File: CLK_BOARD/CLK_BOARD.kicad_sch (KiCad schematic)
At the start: 0 parts

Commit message: updated the symbol in LO board from lmx2582 to lmx2592 in order to cover the upper range of the 5Ghz spectrum. drop in replacement
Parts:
- added C1, C4: 10uF, Capacitor_SMD:C_0603_1608Metric, symbol Device:C
- added C10, C11, C15, C16, C17, C33, C9: 0.1uF, symbol Device:C
- added C12, C31, C7: 10uF, symbol Device:C
- added C13, C32, C8: 1uF, symbol Device:C
- added C14, C18, C19, C22, C23, C24, C25: 10nF, symbol Device:C
- added C2, C30, C5: 0.1uF, Capacitor_SMD:C_0603_1608Metric, symbol Device:C
- added C20, C21, C26, C27: 15pF, symbol Device:C
- added C28, C6: 1uF, Capacitor_SMD:C_0603_1608Metric, symbol Device:C
- added C29: 10nF, Capacitor_SMD:C_0603_1608Metric, symbol Device:C
- added C3: 10nF, Capacitor_SMD:C_0402_1005Metric, symbol Device:C
- added J1: PWR, Connector_PinHeader_2.54mm:PinHeader_1x02_P2.54mm_Vertical, symbol Connector_Generic:Conn_01x02
- added J2, J3, J4, J5, J8: OUT_100M_1, symbol Connector:Conn_Coaxial
- added J6: OUT_100M_3, symbol Connector:Conn_Coaxial
- added J7: OUT_100M_2, symbol Connector:Conn_Coaxial
- added J9: CTRL, symbol Connector_Generic:Conn_01x02
- added R1: 3k16, Resistor_SMD:R_0402_1005Metric, symbol Device:R
- added R10, R11, R12, R5, R6, R7, R9: 43, symbol Device:R
- added R13: 1, Resistor_SMD:R_0603_1608Metric, symbol Device:R
- added R14, R15, R16, R3, R4, R8: 0, symbol Device:R
- added R2: 1k, Resistor_SMD:R_0402_1005Metric, symbol Device:R
- added R26, R27: 10k, Resistor_SMD:R_0603_1608Metric, symbol Device:R
- added U1: TPS7A9101DSKR, Snapeda:DSK0010A, symbol Snapeda:TPS7A9101DSKR
- added U2, U3: LMK00804BPW, Snapeda:PW16_TEX-L, symbol Snapeda:LMK00804BPW
- added U4: SN74LVC1G74DCUR, Snapeda:DCU0008A_L, symbol Snapeda:SN74LVC1G74DCUR
- added X1: TB612-100.0M, Snapeda:TB612_CNW, symbol Snapeda:TB612-100.0M
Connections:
- new net: C28.1, C29.1, C30.1, R13.2, X1.9 (VCC)
- new net: R15.1, U4.7 (PRE_N)
- new net: C13.1, C15.1, C16.1, C17.1, R4.2, U3.11 (VDDO), U3.15 (VDDO), U3.3 (VDD)
- new net: C18.1, J3.1 (In)
- new net: C21.1, R8.2, U4.1 (CLK)
- new net: C19.1, J4.1 (In)
- new net: R7.1, U2.12 (Q2)
- new net: C19.2, R7.2
- new net: C26.1, R14.1, X1.5 (OUTPUT)
- new net: C23.2, J6.1 (In)
- new net: C3.2, R1.2, R2.1, U1.3 (FB)
- new net: C10.1, C11.1, C8.1, C9.1, R3.2, U2.11 (VDDO), U2.15 (VDDO), U2.3 (VDD)
- new net: R5.1, U2.16 (Q0)
- new net: C14.2, R5.2
- new net: C18.2, R6.2
- new net: C25.1, R12.2
- new net: C25.2, J8.1 (In)
- new net: C20.1, R8.1, U3.16 (Q0)
- new net: C32.1, C33.1, R16.2, U4.8 (VCC)
- new net: R9.1, U2.10 (Q3)
- new net: C22.2, R9.2
- new net: C23.1, R10.2
- new net: C24.2, J7.1 (In)
- new net: R11.1, U3.12 (Q2)
- new net: C24.1, R11.2
- new net: C1.1, C2.1, J1.2 (Pin_2), U1.10 (IN), U1.6 (SS_CTRL), U1.7 (EN), U1.9 (IN)
- new net: R12.1, U3.14 (Q1)
- new net: C22.1, J5.1 (In)
- new net: U2.8 (LVCMOS_CLK), U4.2 (D), U4.3 (Q_N)
- new net: C6.1, U1.8 (NR_SS)
- new net: R10.1, U3.10 (Q3)
- new net: R6.1, U2.14 (Q1)
- new net: C14.1, J2.1 (In)
- new net +3V3: C12.1, C3.1, C31.1, C4.1, C5.1, C7.1, R1.1, R13.1, R15.2, R16.1, R26.2, R27.2, R3.1, R4.1, U1.1 (OUT), U1.2 (OUT)
- new net GND: C1.2, C10.2, C11.2, C12.2, C13.2, C15.2, C16.2, C17.2, C2.2, C20.2, C21.2, C26.2, C27.2, C28.2, C29.2, C30.2, C31.2, C32.2, C33.2, C4.2, C5.2, C6.2, C7.2, C8.2, C9.2, J1.1 (Pin_1), J2.2 (Ext), J3.2 (Ext), J4.2 (Ext), J5.2 (Ext), J6.2 (Ext), J7.2 (Ext), J8.2 (Ext), R2.2, U1.11 (PAD), U1.4 (GND), U1.5 (PG), U2.1 (GND), U2.13 (GND), U2.7 (CLK_SEL), U2.9 (GND), U3.1 (GND), U3.13 (GND), U3.7 (CLK_SEL), U3.9 (GND), U4.4 (GND), X1.4 (GND)
- new net OSC_OUT: C27.1, R14.2, U3.8 (LVCMOS_CLK)
- new net nMUTE: J9.1 (Pin_1), R26.1, U2.4 (CLK_EN), U3.4 (CLK_EN)
- new net nRST: J9.2 (Pin_2), R27.1, U4.6 (CLR_N)
- no-connect marks 0 -> 8
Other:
- note added: "POWER SUPPLY SECTION"
- note added: "TCXO SECTION"

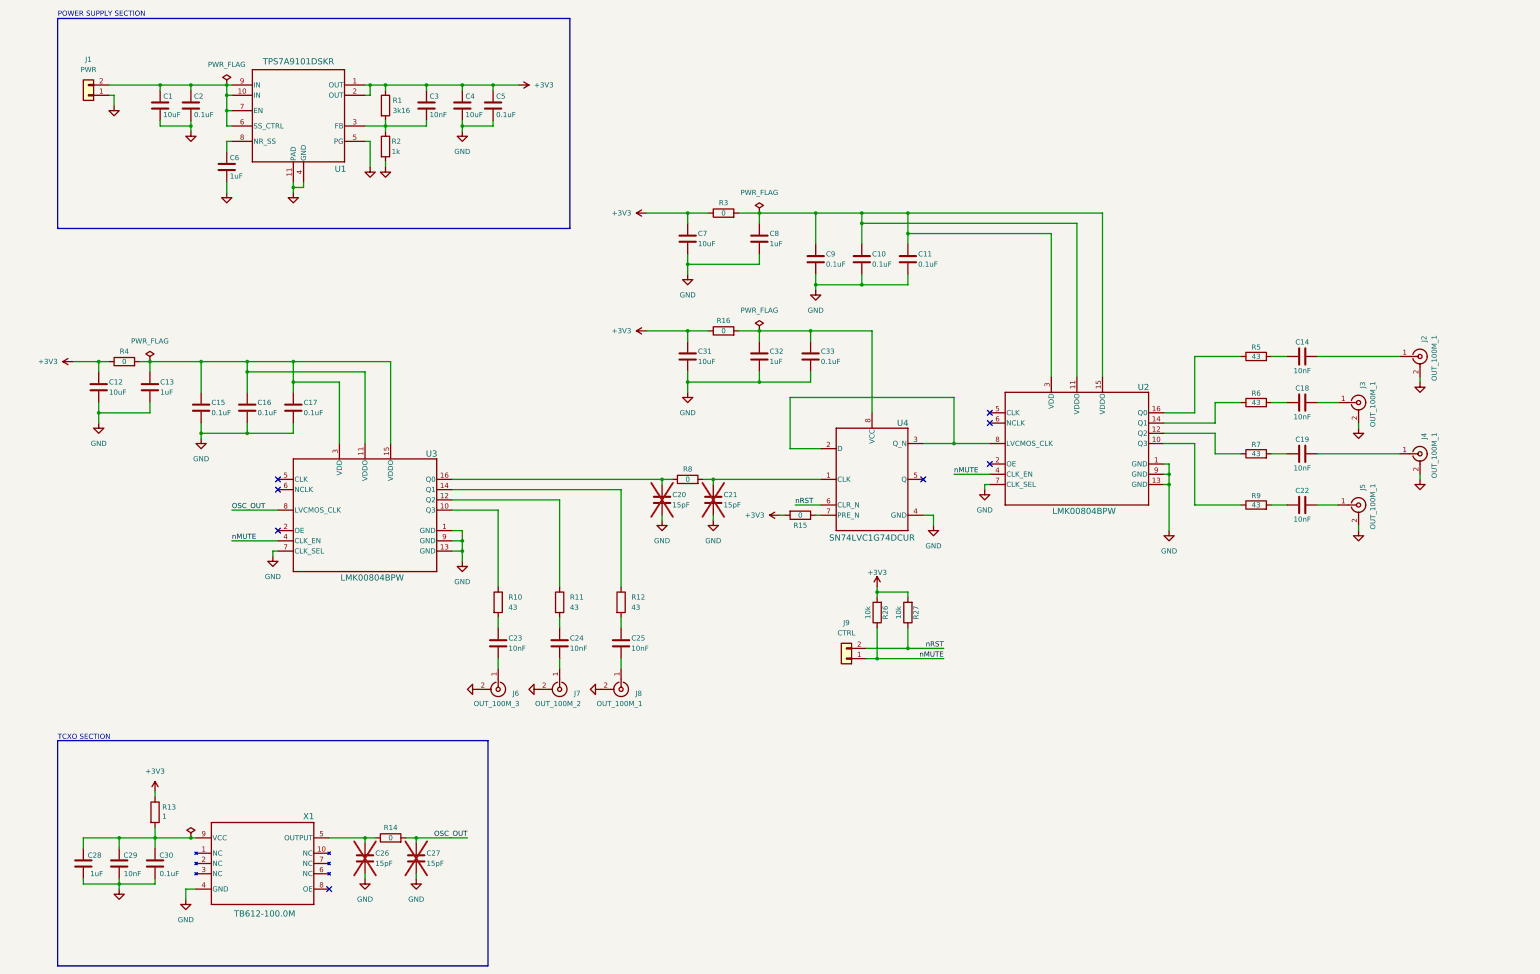
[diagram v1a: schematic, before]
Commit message: finished clock board schematic
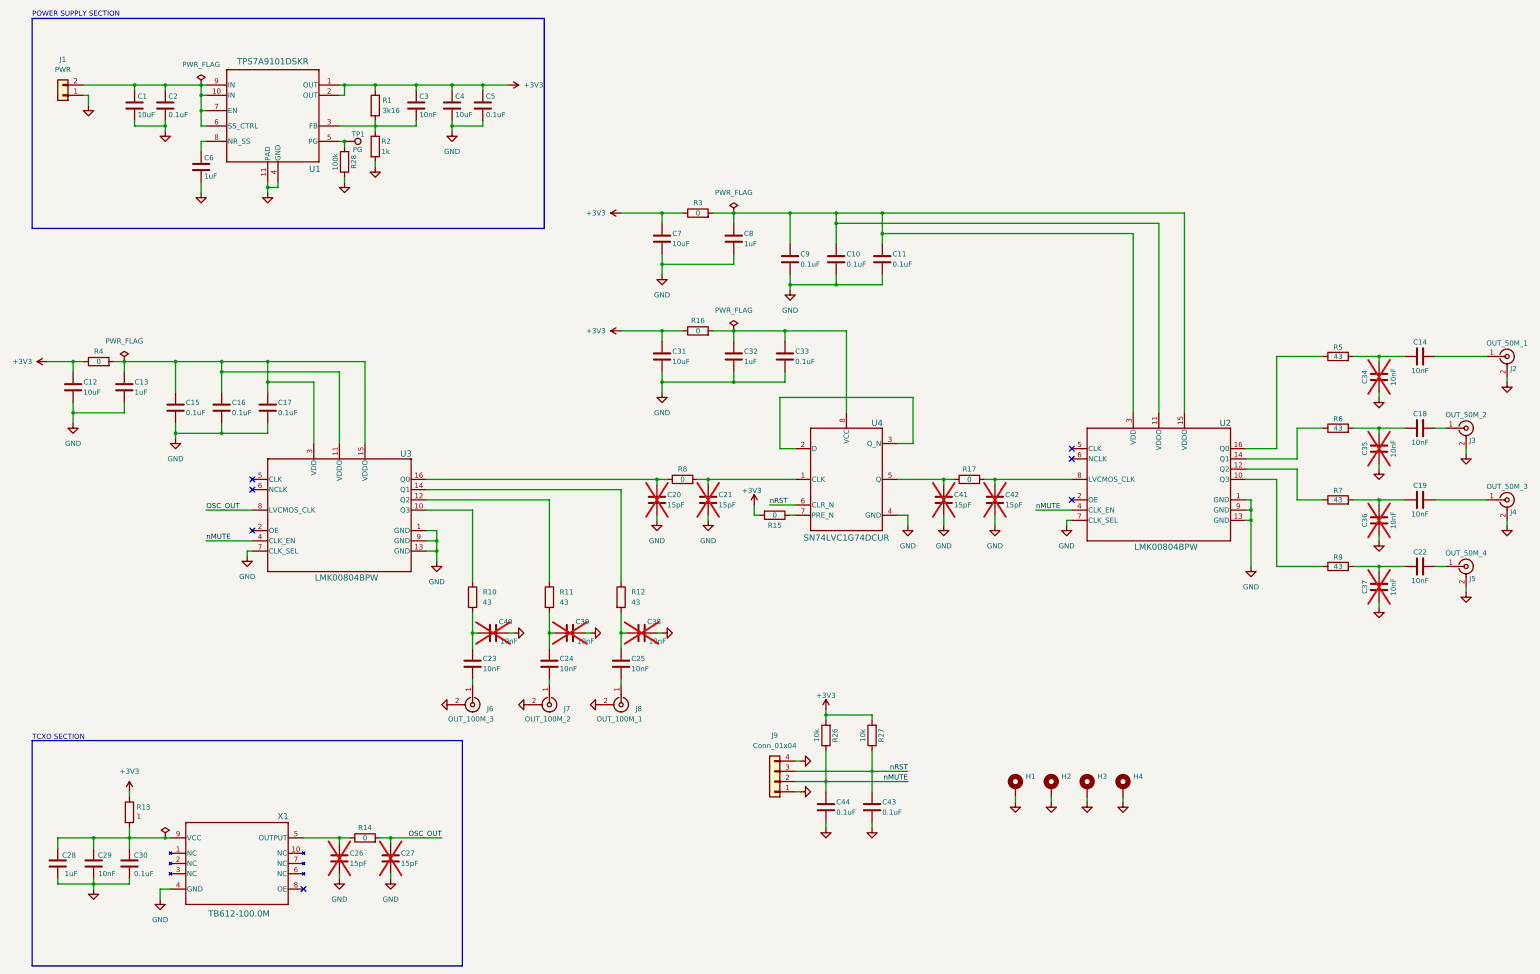
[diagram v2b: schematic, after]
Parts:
- removed J9: CTRL, symbol Connector_Generic:Conn_01x02
- added C34, C35, C36, C37, C38, C39, C40: 10nF, Capacitor_SMD:C_0402_1005Metric, symbol Device:C
- added C41, C42: 15pF, Capacitor_SMD:C_0402_1005Metric, symbol Device:C
- added C43, C44: 0.1uF, Capacitor_SMD:C_0603_1608Metric, symbol Device:C
- added H1, H2, H3, H4: MountingHole_Pad, MountingHole:MountingHole_2.2mm_M2_Pad_Via, symbol Mechanical:MountingHole_Pad
- added J9: Conn_01x04, Connector_PinHeader_2.54mm:PinHeader_1x04_P2.54mm_Vertical, symbol Connector_Generic:Conn_01x04
- added R17: 0, Resistor_SMD:R_0402_1005Metric, symbol Device:R
- added R28: 100k, Resistor_SMD:R_0603_1608Metric, symbol Device:R
- added TP1: PG, TestPoint:TestPoint_Pad_D1.5mm, symbol Connector:TestPoint
- C10, C11, C12, C13, C15, C16, C17, C31, C32, C33, C7, C8, C9: footprint (none) -> Capacitor_SMD:C_0603_1608Metric
- C14, C18, C19, C20, C21, C22, C23, C24, C25, C26, C27: footprint (none) -> Capacitor_SMD:C_0402_1005Metric
- J2: value OUT_100M_1 -> OUT_50M_1; footprint (none) -> Connector_Coaxial:SMA_Samtec_SMA-J-P-H-ST-EM1_EdgeMount
- J3: value OUT_100M_1 -> OUT_50M_2; footprint (none) -> Connector_Coaxial:SMA_Samtec_SMA-J-P-H-ST-EM1_EdgeMount
- J4: value OUT_100M_1 -> OUT_50M_3; footprint (none) -> Connector_Coaxial:SMA_Samtec_SMA-J-P-H-ST-EM1_EdgeMount
- J5: value OUT_100M_1 -> OUT_50M_4; footprint (none) -> Connector_Coaxial:SMA_Samtec_SMA-J-P-H-ST-EM1_EdgeMount
- J6, J7, J8: footprint (none) -> Connector_Coaxial:SMA_Samtec_SMA-J-P-H-ST-EM1_EdgeMount
- R10, R11, R12, R14, R15, R5, R6, R7, R8, R9: footprint (none) -> Resistor_SMD:R_0402_1005Metric
- R16, R3, R4: footprint (none) -> Resistor_SMD:R_0603_1608Metric
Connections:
- net GND: now also C34.2, C35.2, C36.2, C37.2, C38.2, C39.2, C40.2, C41.2, C42.2, C43.2, C44.2, H1.1, H2.1, H3.1, H4.1, J9.1 (Pin_1), J9.4 (Pin_4), R28.1; no longer U1.5 (PG)
- net nMUTE: now also C44.1, J9.2 (Pin_2)
- net nRST: now also C43.1, J9.3 (Pin_3)
- net at C19.2, R7.2: now also C36.1
- net at C14.2, R5.2: now also C34.1
- net at C18.2, R6.2: now also C35.1
- net at C25.1, R12.2: now also C38.1
- net at C22.2, R9.2: now also C37.1
- net at C23.1, R10.2: now also C40.1
- net at C24.1, R11.2: now also C39.1
- net at U4.2 (D), U4.3 (Q_N): no longer U2.8 (LVCMOS_CLK)
- net at U4.5 (Q): now also C41.1, R17.1
- new net: R28.2, TP1.1, U1.5 (PG)
- new net: C42.1, R17.2, U2.8 (LVCMOS_CLK)
- no-connect marks 8 -> 7
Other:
- moved on the sheet: C1, C10, C11, C12, C13, C14, C15, C16, C17, C18, C19, C2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

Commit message: started layout of clk distribution board
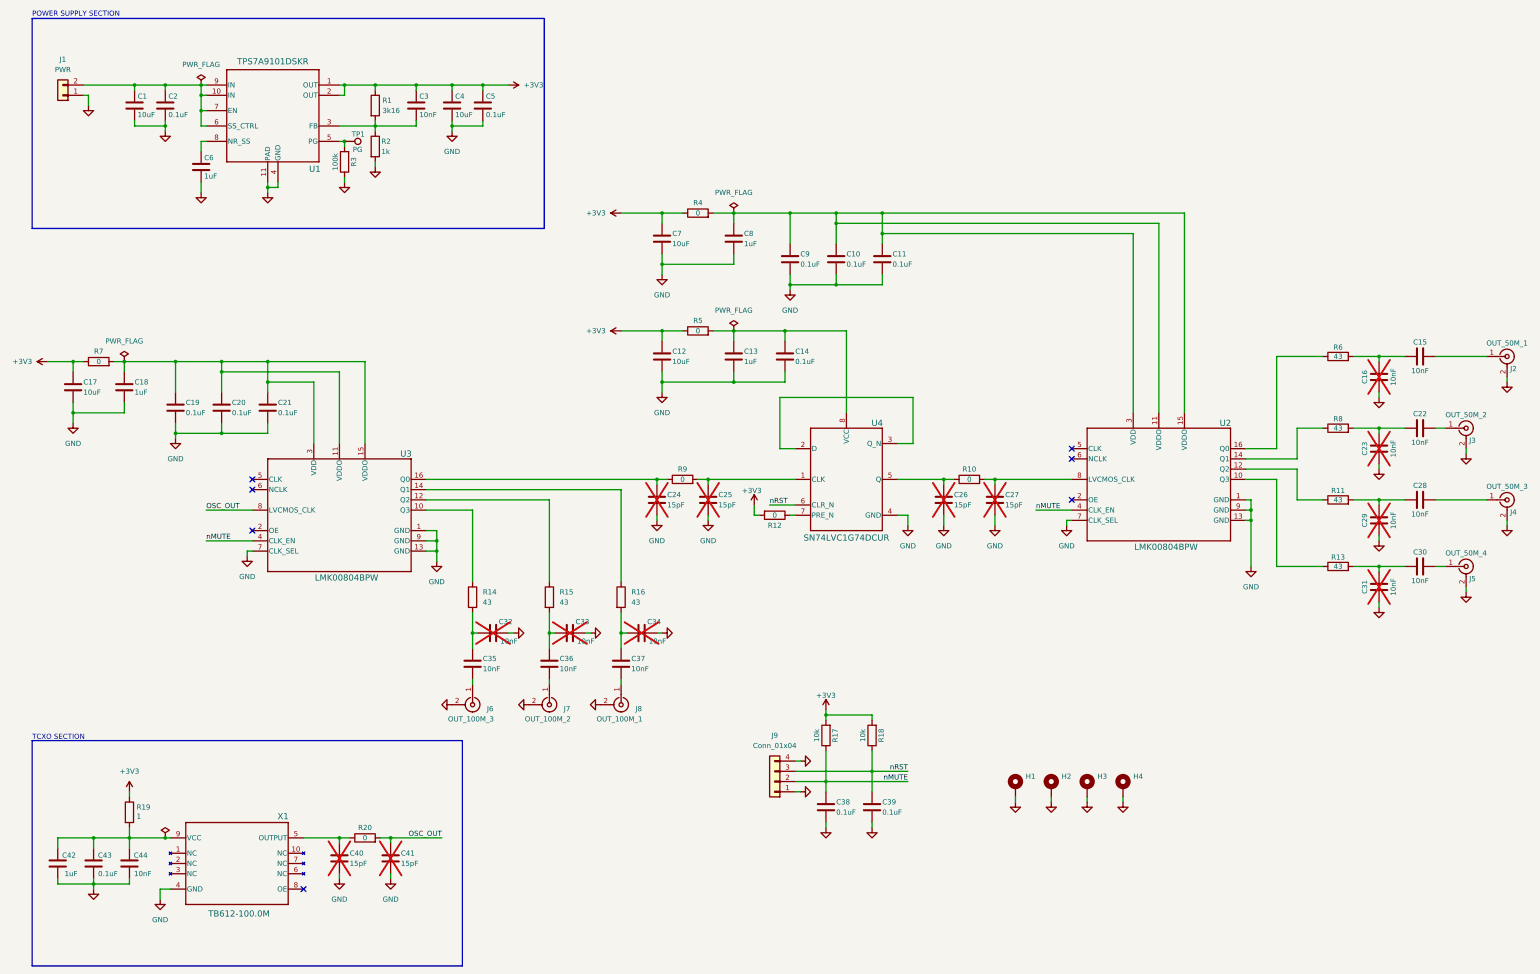
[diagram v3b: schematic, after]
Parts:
- removed C29: 10nF, Capacitor_SMD:C_0603_1608Metric, symbol Device:C
- removed C30: 0.1uF, Capacitor_SMD:C_0603_1608Metric, symbol Device:C
- added C43: 0.1uF, Capacitor_SMD:C_0603_1608Metric, symbol Device:C
- added C44: 10nF, Capacitor_SMD:C_0603_1608Metric, symbol Device:C
- renumbered C31 to C12, C32 to C13, C33 to C14, C14 to C15, C34 to C16, C12 to C17, C13 to C18, C15 to C19, C16 to C20, C17 to C21, C18 to C22, C35 to C23, C20 to C24, C21 to C25, C41 to C26, C42 to C27, C19 to C28, C36 to C29, C22 to C30, C37 to C31, C40 to C32, C39 to C33, C38 to C34, C23 to C35, C24 to C36, C25 to C37, C44 to C38, C43 to C39, C26 to C40, C27 to C41, C28 to C42, R17 to R10, R7 to R11, R15 to R12, R9 to R13, R10 to R14, R11 to R15, R12 to R16, R26 to R17, R27 to R18, R13 to R19, R14 to R20, R28 to R3, R3 to R4, R16 to R5, R5 to R6, R4 to R7, R6 to R8, R8 to R9
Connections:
- net GND: now also C43.2, C44.2
- net at C42.1, R19.2, X1.9 (VCC): now also C43.1, C44.1

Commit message: moved from TSSOP to QFN to make the pcb smaller, will have to restart layout
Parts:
- U2, U3: value LMK00804BPW -> LMK00804BQWRGTRQ1; footprint Snapeda:PW16_TEX-L -> Snapeda:VQFN16_RGT_TEX; symbol Snapeda:LMK00804BPW -> Snapeda:LMK00804BQWRGTRQ1
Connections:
- net GND: now also U2.17 (PAD), U3.17 (PAD)
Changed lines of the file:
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@@
 	)
 	(junction
+		(at 331.47 151.13)
+		(diameter 0)
+		(color 0 0 0 0)
+	)
+	(junction
 		(at 106.68 54.61)
 		(diameter 0)
@@
 	)
 	(junction
+		(at 129.54 158.75)
+		(diameter 0)
+		(color 0 0 0 0)
+	)
+	(junction
 		(at 228.6 90.17)
 		(diameter 0)
@@
 	(wire
 		(pts
+			(xy 330.2 151.13) (xy 331.47 151.13)
+		)
+		(stroke
+			(width 0)
+			(type default)
+		)
+	)
+	(wire
+		(pts
 			(xy 228.6 74.93) (xy 228.6 80.01)
 		)
@@
 	(wire
 		(pts
+			(xy 127 158.75) (xy 129.54 158.75)
+		)
+		(stroke
+			(width 0)
+			(type default)
+		)
+	)
+	(wire
+		(pts
 			(xy 52.07 109.22) (xy 52.07 111.76)
 		)
@@
 	)
 	(symbol
-		(lib_name "LMK00804BPW_1")
-		(lib_id "Snapeda:LMK00804BPW")
+		(lib_id "Snapeda:LMK00804BQWRGTRQ1")
 		(at 80.01 138.43 0)
 		(unit 1)
@@
 			)
 		)
-		(property "Value" "LMK00804BPW"
+		(property "Value" "LMK00804BQWRGTRQ1"
 			(at 107.188 162.814 0)
 			(show_name no)
@@
 			)
 		)
-		(property "Footprint" "Snapeda:PW16_TEX-L"
+		(property "Footprint" "Snapeda:VQFN16_RGT_TEX"
 			(at 79.248 109.728 0)
 			(hide yes)
@@
 			)
 		)
-		(property "Datasheet" "https://www.ti.com/lit/gpn/lmk00804b"
+		(property "Datasheet" "https://www.ti.com/lit/gpn/lmk00804b-q1"
 			(at 79.248 112.268 0)
 			(hide yes)
@@
 		(pin "2"
 		)
+		(pin "17"
+		)
 		(instances
 			(project "CLK_BOARD"
@@
 	)
 	(symbol
-		(lib_name "LMK00804BPW_1")
-		(lib_id "Snapeda:LMK00804BPW")
+		(lib_id "Snapeda:LMK00804BQWRGTRQ1")
 		(at 283.21 130.81 0)
 		(unit 1)
@@
 			)
 		)
-		(property "Value" "LMK00804BPW"
+		(property "Value" "LMK00804BQWRGTRQ1"
 			(at 310.388 155.194 0)
 			(show_name no)
@@
 			)
 		)
-		(property "Footprint" "Snapeda:PW16_TEX-L"
+		(property "Footprint" "Snapeda:VQFN16_RGT_TEX"
 			(at 282.448 102.108 0)
 			(hide yes)
@@
 			)
 		)
-		(property "Datasheet" "https://www.ti.com/lit/gpn/lmk00804b"
+		(property "Datasheet" "https://www.ti.com/lit/gpn/lmk00804b-q1"
 			(at 282.448 104.648 0)
 			(hide yes)
@@
 		(pin "2"
 		)
+		(pin "17"
+		)
 		(instances
